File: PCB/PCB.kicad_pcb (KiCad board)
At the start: 2 copper layers, 80 x 46 mm, 7 parts, among them J1 Lidar_1, J2 Lidar_2, J3 Lidar_3, J6 Buzzer, U1 Teensy4.0

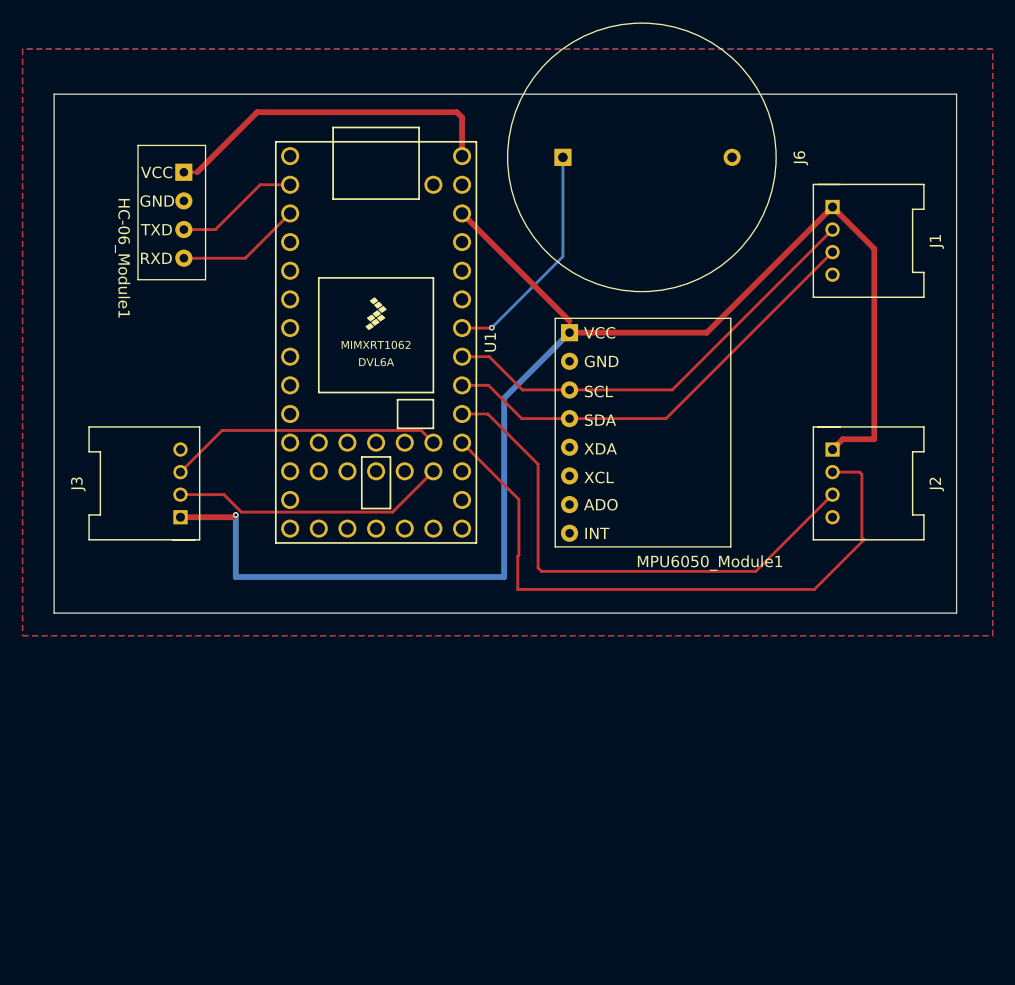
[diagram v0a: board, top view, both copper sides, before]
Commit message: add pullups and second IMU
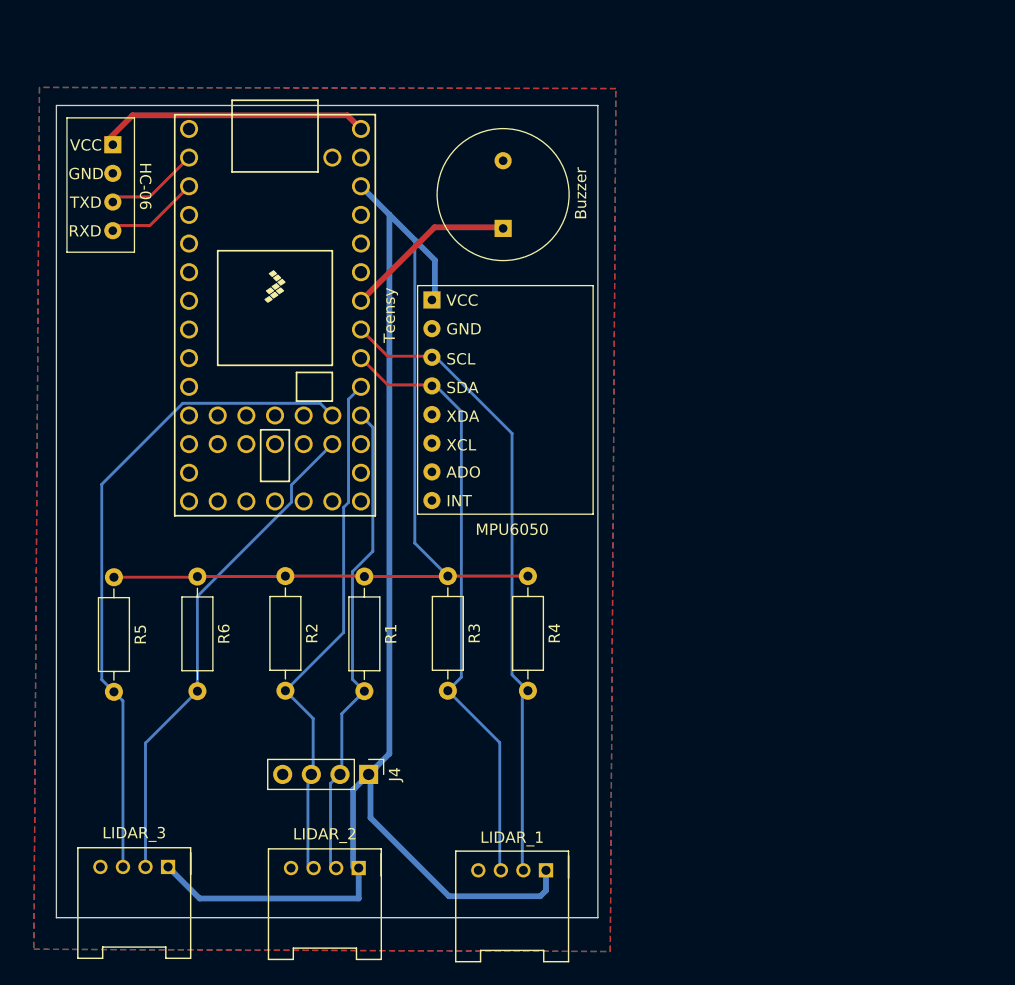
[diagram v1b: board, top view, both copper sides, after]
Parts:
- added J4: IMU_2, Connector_PinHeader_2.54mm:PinHeader_1x04_P2.54mm_Vertical, F.Cu at (92.7, 119.3)
- added R1: 4.7k, Resistor_THT:R_Axial_DIN0207_L6.3mm_D2.5mm_P10.16mm_Horizontal, F.Cu at (92.3, 101.8)
- added R2: 4.7k, Resistor_THT:R_Axial_DIN0207_L6.3mm_D2.5mm_P10.16mm_Horizontal, F.Cu at (85.3, 101.7)
- added R3: 4.7k, Resistor_THT:R_Axial_DIN0207_L6.3mm_D2.5mm_P10.16mm_Horizontal, F.Cu at (99.7, 101.7)
- added R4: 4.7k, Resistor_THT:R_Axial_DIN0207_L6.3mm_D2.5mm_P10.16mm_Horizontal, F.Cu at (106.8, 101.7)
- added R5: 4.7k, Resistor_THT:R_Axial_DIN0207_L6.3mm_D2.5mm_P10.16mm_Horizontal, F.Cu at (70.1, 101.8)
- added R6: 4.7k, Resistor_THT:R_Axial_DIN0207_L6.3mm_D2.5mm_P10.16mm_Horizontal, F.Cu at (77.5, 101.8)
- Buzzer: renamed from J6; footprint Customs:Buzzer -> Customs:Small_Buzzer
- Teensy: renamed from U1; footprint teensy.pretty-master:Teensy40 -> teensy:Teensy40
- moved LIDAR_1 66.9 mm to (105.4, 131.0), turned to 180 degrees
- moved LIDAR_2 60.9 mm to (88.8, 130.8), turned to 180 degrees
- moved LIDAR_3 37.2 mm to (71.9, 130.7), turned to 180 degrees
- moved Buzzer 12.7 mm to (104.6, 67.9)
- moved MPU6050 12.5 mm to (104.6, 83.6)
- moved Teensy 9.28 mm to (84.4, 78.6)
- moved HC-06 6.76 mm to (68.5, 67.2)
- renumbered HC-06_Module1 to HC-06, J1 to LIDAR_1, J2 to LIDAR_2, J3 to LIDAR_3, MPU6050_Module1 to MPU6050
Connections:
- MPU6050 pad 7: unconnected-(MPU6050_Module1-ADO-Pad7) -> GND
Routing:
- net +3V3: track 127.0 -> 187.0 mm, vias 1 -> 0
- net Net-(J3-Pin_3): track 24.4 -> 58.6 mm
- net Net-(J3-Pin_2): track 24.6 -> 44.3 mm
- net Net-(J1-Pin_2): track 40.0 -> 56.4 mm
- net Net-(J1-Pin_3): track 40.2 -> 53.6 mm
- net Net-(J2-Pin_2): track 56.2 -> 42.9 mm
- net +5V: track 30.5 -> 23.8 mm
- net Net-(J6-Pin_1): track 20.4 -> 15.8 mm, vias 1 -> 0
- net Net-(HC-06_Module1-TXD): track 11.1 -> 8.60 mm
- net Net-(HC-06_Module1-RXD): track 11.1 -> 8.60 mm
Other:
- board size 80 x 46 mm -> 48 x 72 mm
- copper layers 2 -> 4
- rule pad_to_mask_clearance: 0.0508 -> 0

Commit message: mounting holes + vias, extra route for last I2C port
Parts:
- added REF**: MountingHole_3.2mm_M3, MountingHole:MountingHole_3.2mm_M3, F.Cu at (67.9, 122.0)
- added REF**: MountingHole_3.2mm_M3, MountingHole:MountingHole_3.2mm_M3, F.Cu at (67.9, 64.0)
- added REF**: MountingHole_3.2mm_M3, MountingHole:MountingHole_3.2mm_M3, F.Cu at (109.5, 89.3)
- added REF**: MountingHole_3.2mm_M3, MountingHole:MountingHole_3.2mm_M3, F.Cu at (109.5, 122.0)
- added REF**: MountingHole_3.2mm_M3, MountingHole:MountingHole_3.2mm_M3, F.Cu at (67.9, 89.3)
- added REF**: MountingHole_3.2mm_M3, MountingHole:MountingHole_3.2mm_M3, F.Cu at (109.5, 64.0)
- moved HC-06 6.30 mm to (68.5, 73.5)
- moved Buzzer 3.50 mm to (101.1, 67.9)
- renumbered LIDAR_1 to Lidar_1, LIDAR_2 to Lidar_2, LIDAR_3 to Lidar_3
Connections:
- Teensy pad 43: unconnected-(U1-32_OUT1B-Pad43) -> Net-(J3-Pin_2)
- Teensy pad 44: unconnected-(U1-33_MCLK2-Pad44) -> Net-(J3-Pin_3)
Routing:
- net Net-(J3-Pin_2): track 44.3 -> 52.4 mm
- net Net-(HC-06_Module1-RXD): track 8.60 -> 14.8 mm
- net Net-(HC-06_Module1-TXD): track 8.60 -> 13.1 mm
- net Net-(J6-Pin_1): track 15.8 -> 11.8 mm
- net Net-(J3-Pin_3): track 58.6 -> 61.6 mm
- net +5V: track 23.8 -> 25.9 mm
- net GND: vias 0 -> 37
